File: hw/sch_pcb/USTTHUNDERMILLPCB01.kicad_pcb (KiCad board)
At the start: 4 copper layers, 80 x 80 mm, 84 parts, among them J1 SM06B-GHS-TB, J2 SM03B-GHS-TB, J4 HEADER_2x03, J5 SM08B-GHS-TB, J6 SM06B-GHS-TB, SW1 KMT031 NGJ LHS C&K, U1 ISL21080DIH312Z-TK 1V25, U10 SN74LVC1G14QDCKRQ1, U11 SN74LVC1G14QDCKRQ1, U12 SN74LVC1G14QDCKRQ1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

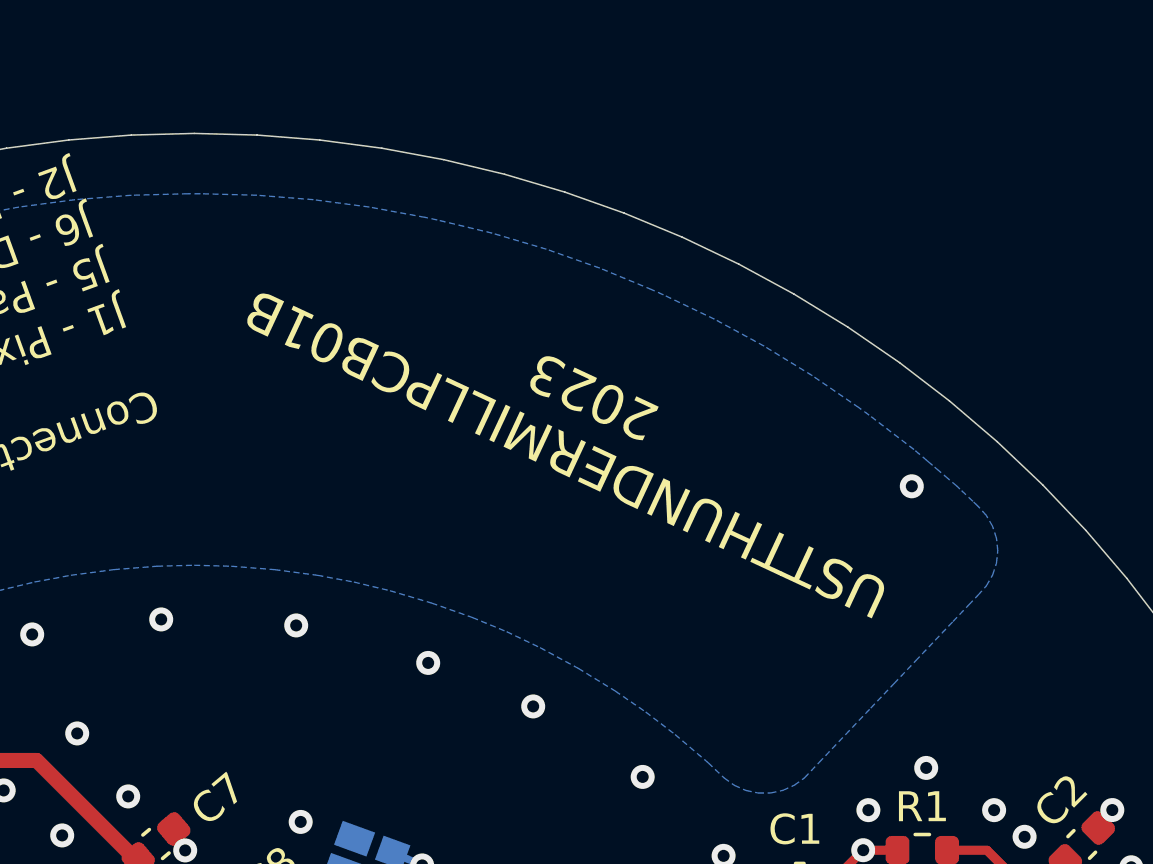
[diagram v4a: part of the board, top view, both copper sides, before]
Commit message: add logo
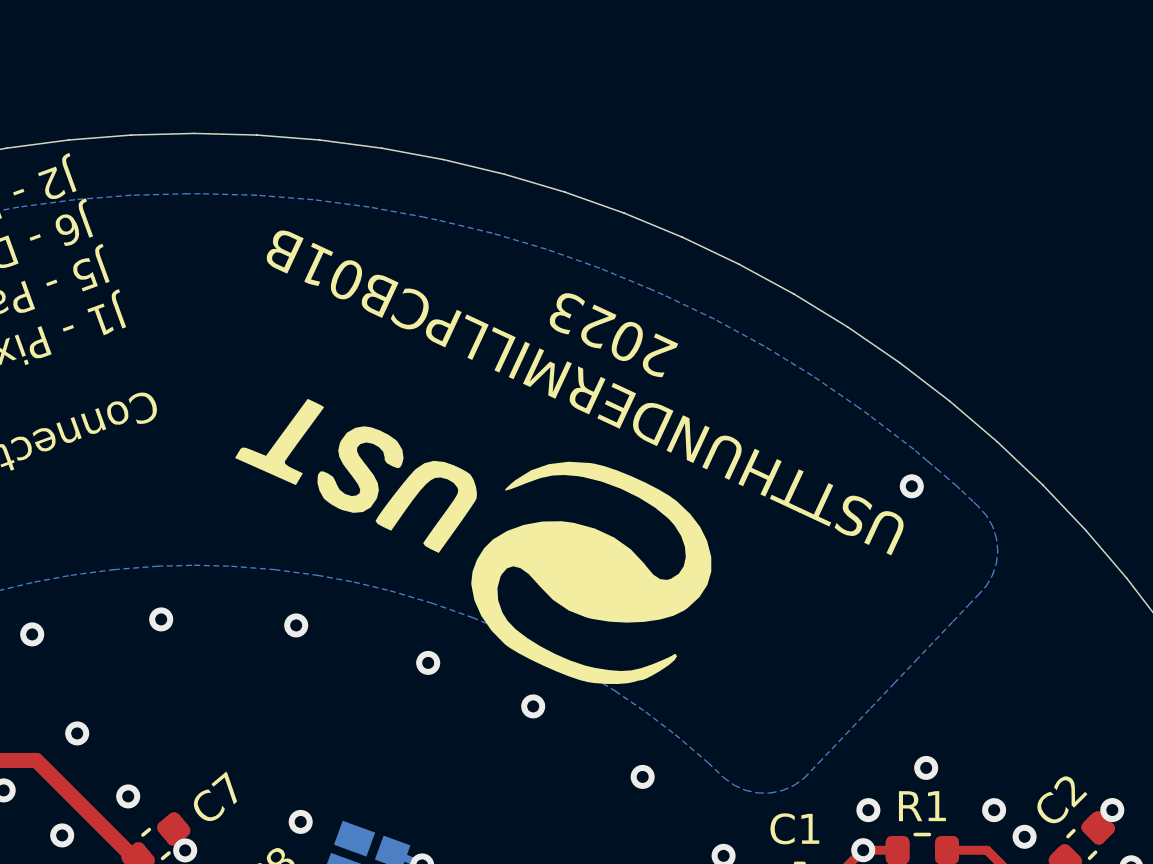
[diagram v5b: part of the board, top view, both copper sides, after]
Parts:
- added G1: , MLAB_LOGA:UST, B.Cu at (171.7, 92.6)
- added G2: , MLAB_LOGA:UST, F.Cu at (151.8, 65.3)

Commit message: analogue power
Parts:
- added C26: 100nF, Capacitor_SMD:C_0603_1608Metric, F.Cu at (174.3, 88.1)
- added JP4: Jumper_2_Bridged, NetTie:NetTie-2_SMD_Pad0.5mm, F.Cu at (158.2, 102.8)
- moved D2 23.6 mm to (140.1, 71.5), turned to 135 degrees
- moved R1 19.3 mm to (174.6, 94.0)
- moved C1 19.1 mm to (167.9, 95.7), turned to -90 degrees
- moved F1 18.3 mm to (137.4, 74.0), turned to -45 degrees
- moved C9 17.7 mm to (163.1, 100.4), turned to 180 degrees
- moved U1 17.5 mm to (170.4, 95.9), turned to -90 degrees
- moved C10 17.4 mm to (163.3, 102.3), turned to 180 degrees
- moved C2 17.2 mm to (177.7, 92.5), turned to 180 degrees
- moved D1 16.5 mm to (176.9, 94.6), turned to -90 degrees
- moved U2 12.8 mm to (174.3, 91.1), turned to 90 degrees
- moved C5 11.2 mm to (174.4, 86.4), turned to 180 degrees
- moved R2 9.66 mm to (166.7, 92.3), turned to 90 degrees
- moved J2 9.51 mm to (163.8, 88.2), turned to 180 degrees
- moved C3 9.30 mm to (165.2, 93.9), turned to 90 degrees
- moved C4 9.21 mm to (170.0, 91.7), turned to -90 degrees
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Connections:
- C1 pad 2: ROTOR_GND -> GNDA
- C10 pad 1: +3.3VP -> +3.3VA
- C10 pad 2: ROTOR_GND -> GNDA
- C16 pad 1: /CPU/AVCC -> +3.3VA
- C16 pad 2: ROTOR_GND -> GNDA
- C21 pad 2: ROTOR_GND -> GNDA
- C23 pad 2: ROTOR_GND -> GNDA
- C3 pad 1: ROTOR_GND -> GNDA
- C5 pad 1: ROTOR_GND -> GNDA
- C5 pad 2: +3.3VP -> +3.3VA
- C9 pad 1: +3.3VP -> +3.3VA
- C9 pad 2: ROTOR_GND -> GNDA
- D1 pad 2: ROTOR_GND -> GNDA
- J2 pad 3: ROTOR_GND -> GNDA
- J2 pad MP: ROTOR_GND -> GNDA
- L1 pad 2: /CPU/AVCC -> +3.3VA
- R4 pad 1: +3.3VP -> unconnected-(R4-Pad1)
- R4 pad 2: +3V3 -> unconnected-(R4-Pad2)
- U1 pad 1: +3.3VP -> +3.3VA
- U1 pad 3: ROTOR_GND -> GNDA
- U2 pad 2: ROTOR_GND -> GNDA
- U2 pad 5: +3.3VP -> +3.3VA
- U8 pad 27: /CPU/AVCC -> +3.3VA
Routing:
- net Net-(D2-K): track 32.9 -> 12.0 mm
- net +5V: track 37.0 -> 56.5 mm, vias 2 -> 3
- net PA1: track 45.2 -> 32.1 mm, vias 6 -> 2
- net +3.3VP: track 12.8 -> 0.00 mm
- net PA0: track 35.4 -> 26.6 mm
- net /CPU/AVCC: track 8.79 -> 0.00 mm
- net +3.3VA: track 0.00 -> 7.58 mm
- net Net-(U2--): track 8.61 -> 5.51 mm
- net +3V3: track 198.0 -> 195.1 mm
- net Net-(D1-A1): track 7.63 -> 4.86 mm
- net STATOR: track 2.49 -> 0.64 mm
- net /CPU/PB5: track 12.4 -> 13.7 mm
- net /CPU/RST#_P: track 19.1 -> 18.4 mm
- net /CPU/BTN: track 24.7 -> 24.2 mm
- net ROTOR_GND: track 4.64 -> 4.43 mm, vias 210 -> 29
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- added copper zone on F.Cu, net GNDA
- added copper zone on In1.Cu, net GNDA
